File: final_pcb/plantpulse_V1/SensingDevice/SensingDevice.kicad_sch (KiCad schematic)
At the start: 7 parts, among them J1 SEN0193, J2 LiPo Battery, U2 SHT31-DIS-B2.5KS

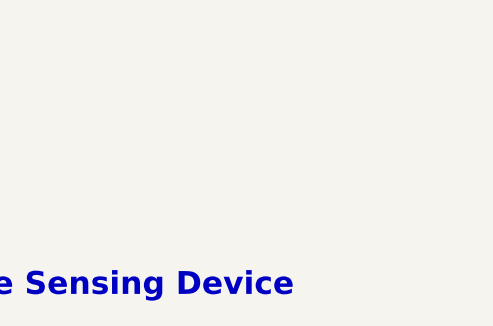
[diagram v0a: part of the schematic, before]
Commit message: src code for sensing device update
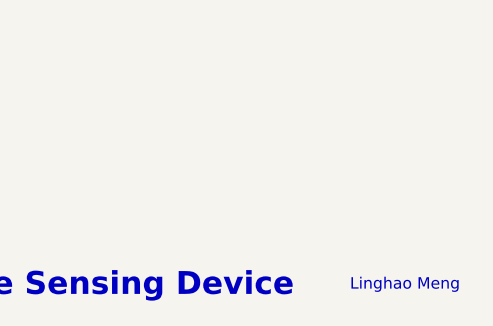
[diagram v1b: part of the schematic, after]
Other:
- note added: "Linghao Meng"
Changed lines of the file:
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@@
 	(generator_version "9.0")
 	(paper "A4")
+	(text "Linghao Meng"
+		(exclude_from_sim no)
+		(at 264.668 174.498 0)
+		(effects
+			(font
+				(size 1.27 1.27)
+			)
+		)
+	)
 	(text "PlantPulse Sensing Device"
 		(exclude_from_sim no)
